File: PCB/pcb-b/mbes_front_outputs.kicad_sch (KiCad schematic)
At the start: 56 parts, among them Q1 BC817, Q11 TPCA8120,L1Q, Q14 BC817, Q15 BC817, Q19 BC817, Q2 BC817, Q20 BC817, Q21 BC817, Q4 TPCA8120,L1Q, Q5 TPCA8120,L1Q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

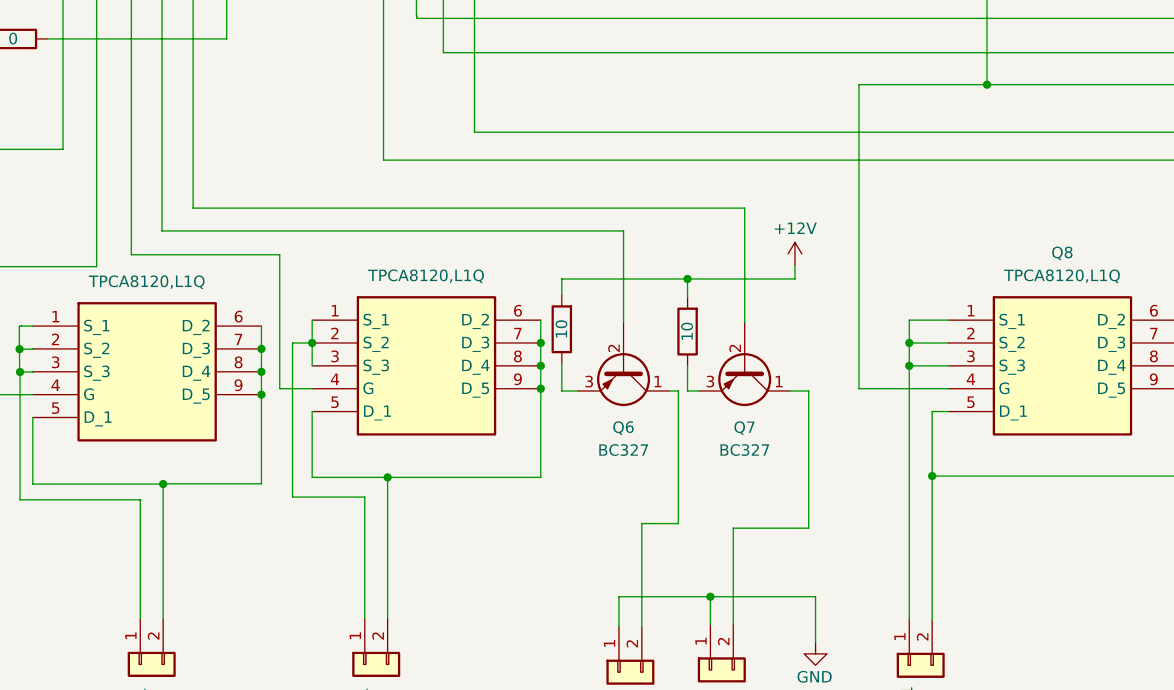
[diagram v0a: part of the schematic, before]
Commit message: Enhancement for direction-indicators circuit
To make the circuit completely safe, I have added MSMF050-2 restatable-fuses to protect it vs short-circuits events.
In order to prevent PNP transistors damages, I have also added a 3 Ohm 0.5W resistor composed by four 1206 SMD componets
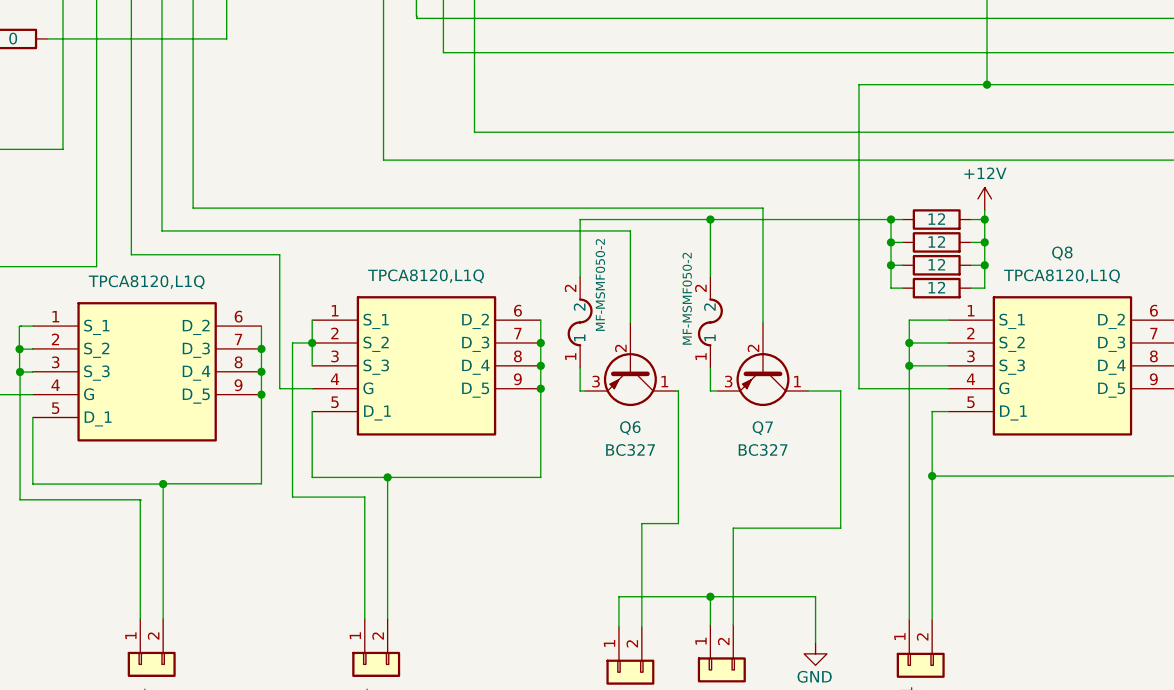
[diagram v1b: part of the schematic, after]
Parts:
- added F1, F2: MF-MSMF050-2, MSMF050-2:FUSE_F050-2, symbol MSMF050-2:MF-MSMF050-2
- added RA30, RA31: 12, Resistor_SMD:R_1206_3216Metric, symbol Device:R
- RA23, RA29: value 10 -> 12; footprint Resistor_THT:R_Axial_DIN0309_L9.0mm_D3.2mm_P12.70mm_Horizontal -> Resistor_SMD:R_1206_3216Metric
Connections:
- net +12V: now also RA30.2, RA31.2
- net at RA23.1: now also RA29.1, F1.2, F2.2, RA30.1, RA31.1; no longer Q7.3 (E)
- net at Q6.3 (E): now also F1.1; no longer RA29.1
- new net: F2.1, Q7.3 (E)
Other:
- moved on the sheet: Q6, Q7

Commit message: Fixes and changes
- 8pin pin-header connectors have been replaced with more standard 10pin connectors
- Wrong components sizes have been fixed
- too small solder-wire connectors have been fixed
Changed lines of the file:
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@@
 (kicad_sch
-	(version 20231120)
+	(version 20250114)
 	(generator "eeschema")
-	(generator_version "8.0")
+	(generator_version "9.0")
 	(paper "A4")
+	(text "LED's resistor depends by the\nled type you are using"
+		(exclude_from_sim no)
+		(at 47.7012 41.5544 90)
+		(effects
+			(font
+				(size 1 1)
+				(italic yes)
+			)
+			(justify left bottom)
+		)
+	)
+	(text "1) addLight\n2) upLight\n3) downLight\n4) leftArrow\n5) rightArrow\n6) neutral\n7) NC\n8) +12V"
+		(exclude_from_sim no)
+		(at 17.145 61.341 0)
+		(effects
+			(font
+				(size 1.27 1.27)
+			)
+			(justify left bottom)
+		)
+	)
 	(junction
 		(at 187.452 76.9112)
@@
 		)
 	)
-	(text "LED's resistor depends by the\nled type you are using"
-		(exclude_from_sim no)
-		(at 47.7012 41.5544 90)
-		(effects
-			(font
-				(size 1 1)
-				(italic yes)
-			)
-			(justify left bottom)
-		)
-	)
-	(text "1) addLight\n2) upLight\n3) downLight\n4) leftArrow\n5) rightArrow\n6) neutral\n7) NC\n8) +12V"
-		(exclude_from_sim no)
-		(at 17.145 61.341 0)
-		(effects
-			(font
-				(size 1.27 1.27)
-			)
-			(justify left bottom)
-		)
-	)

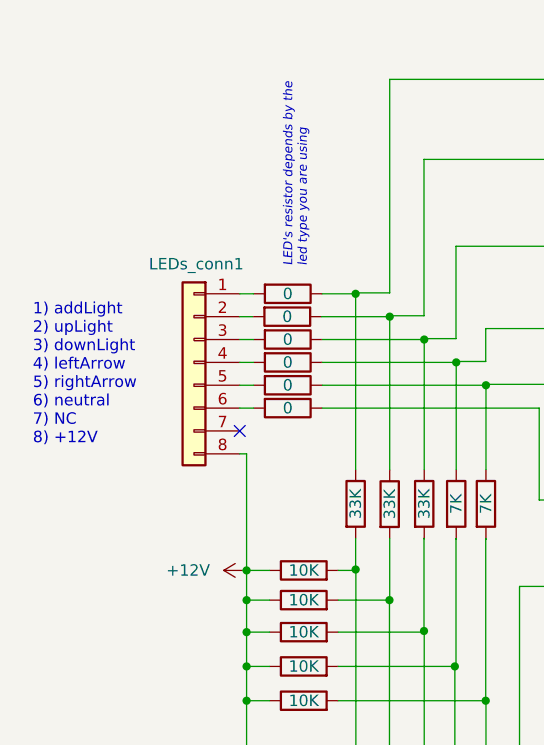
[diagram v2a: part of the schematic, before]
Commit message: Fix: not common connector has been replaced
The 8-pin flat-cable connector is not easy to find on market. It has been replaced with the 10-pin standard one
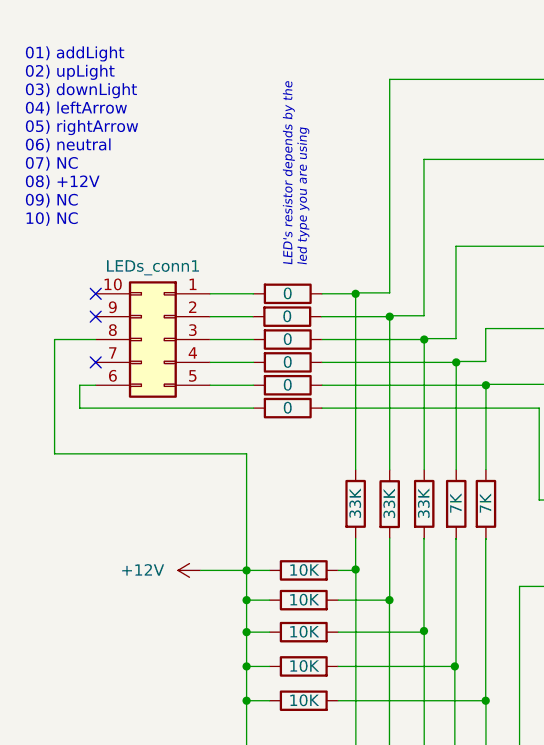
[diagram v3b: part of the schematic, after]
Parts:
- removed LEDs_conn1: Conn_01x08, Connector_PinHeader_2.54mm:PinHeader_2x04_P2.54mm_Vertical, symbol Connector_Generic:Conn_01x08
- added LEDs_conn1: Conn_02x05_Counter_Clockwise, Connector_PinHeader_2.54mm:PinHeader_2x05_P2.54mm_Vertical, symbol Connector_Generic:Conn_02x05_Counter_Clockwise
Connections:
- net +12V: now also LEDs_conn1.8 (Pin_8)
- net at RA1.2: now also LEDs_conn1.1 (Pin_1)
- net at RA2.2: now also LEDs_conn1.2 (Pin_2)
- net at RA3.2: now also LEDs_conn1.3 (Pin_3)
- net at RA4.2: now also LEDs_conn1.4 (Pin_4)
- net at RA5.2: now also LEDs_conn1.5 (Pin_5)
- net at RA6.2: now also LEDs_conn1.6 (Pin_6)
- no-connect marks 1 -> 3
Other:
- note added: "01) addLight 02) upLight 03) downLight 04) leftArrow 05) rightArrow 06) neutral 07) NC 08) +12V 09) NC 10) NC"
- note removed: "1) addLight 2) upLight 3) downLight 4) leftArrow 5) rightArrow 6) neutral 7) NC 8) +12V"

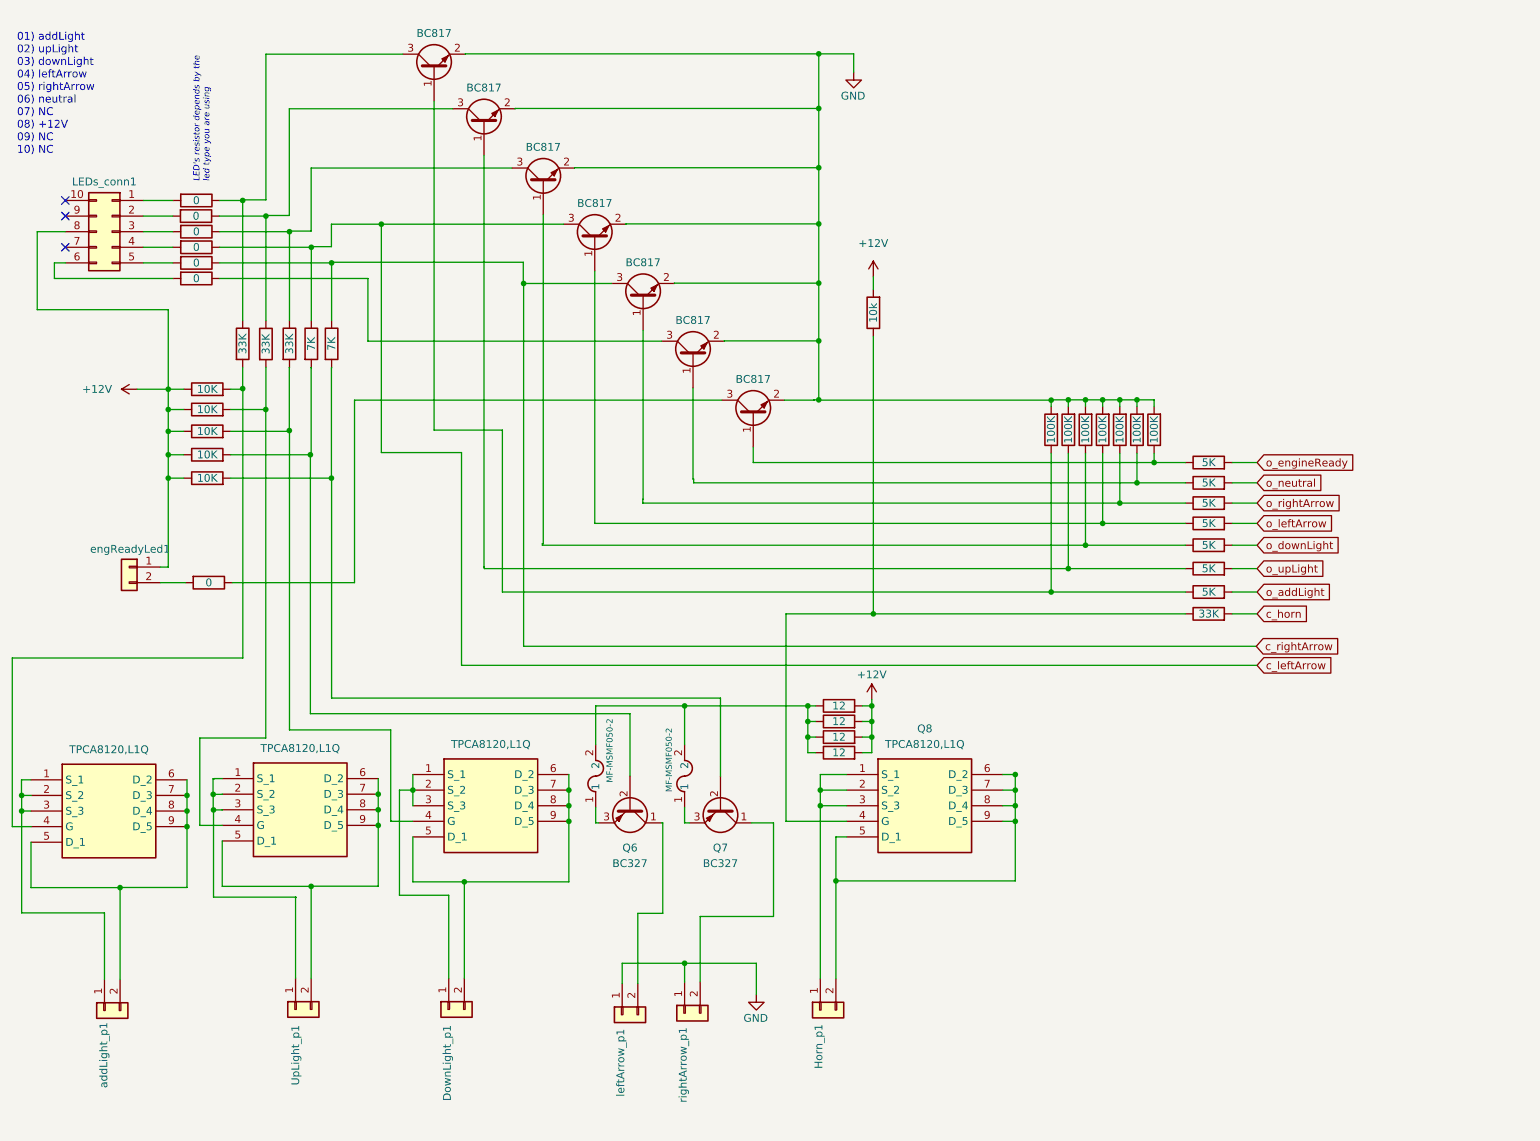
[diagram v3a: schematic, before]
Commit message: Fix stupid error on the direction indicators management
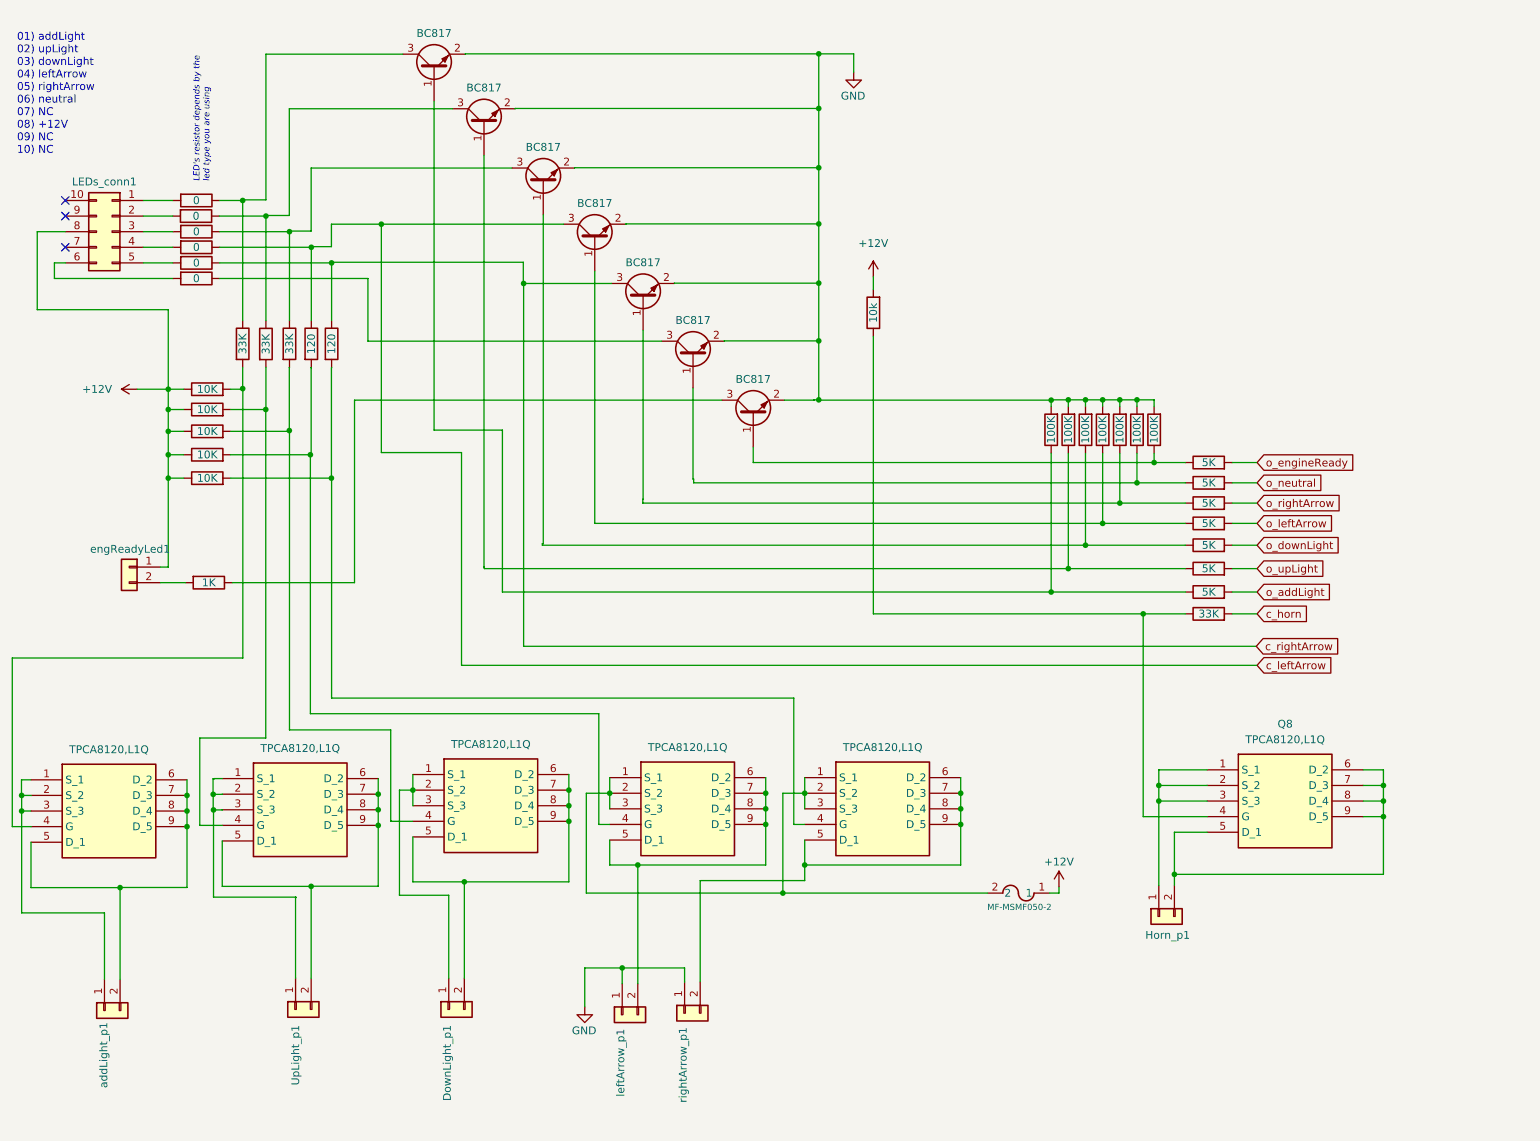
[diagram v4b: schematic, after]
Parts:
- removed F1: MF-MSMF050-2, MSMF050-2:FUSE_F050-2, symbol MSMF050-2:MF-MSMF050-2
- removed Q6, Q7: BC327, Package_TO_SOT_THT:TO-92_Inline_Wide, symbol Transistor_BJT:BC327
- removed RA23, RA29, RA30, RA31: 12, Resistor_SMD:R_1206_3216Metric, symbol Device:R
- added Q6, Q7: TPCA8120,L1Q, TPCA80120:TPH4R003NLL1Q, symbol TPCA8120-LQ:TPCA8120,L1Q
- Q11, Q4, Q5, Q8: footprint TPCA8120:TPH4R003NLL1Q -> TPCA80120:TPH4R003NLL1Q
- RA13, RA14: value 7K -> 120
- RA9: value 0 -> 1K
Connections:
- net +12V: now also F2.1
- net at F2.2: now also Q6.1 (S_1), Q6.2 (S_2), Q6.3 (S_3), Q7.1 (S_1), Q7.2 (S_2), Q7.3 (S_3)
- net at rightArrow_p1.2 (Pin_2): now also Q7.5 (D_1), Q7.6 (D_2), Q7.7 (D_3), Q7.8 (D_4), Q7.9 (D_5)
- net at RA13.2, RA27.2: now also Q6.4 (G)
- net at RA14.2, RA28.2: now also Q7.4 (G)
- net at leftArrow_p1.2 (Pin_2): now also Q6.5 (D_1), Q6.6 (D_2), Q6.7 (D_3), Q6.8 (D_4), Q6.9 (D_5)
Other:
- moved on the sheet: Horn_p1, Q8

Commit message: Fix: horn still usable also when the mb is off
Horn is enabled by tempPower, now
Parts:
- added Q10: BC817, Package_TO_SOT_SMD:SOT-23, symbol Transistor_BJT:BC817
- added RA23: 20K, Resistor_SMD:R_1206_3216Metric, symbol Device:R
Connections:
- net c_horn: now also Q10.2 (E); no longer RA7.2
- net at Q8.4 (G), RA7.1: no longer RA42.1
- new net: Q10.3 (C), RA42.1, RA7.2
- new net: Q10.1 (B), RA23.2
- new net tempPower: RA23.1

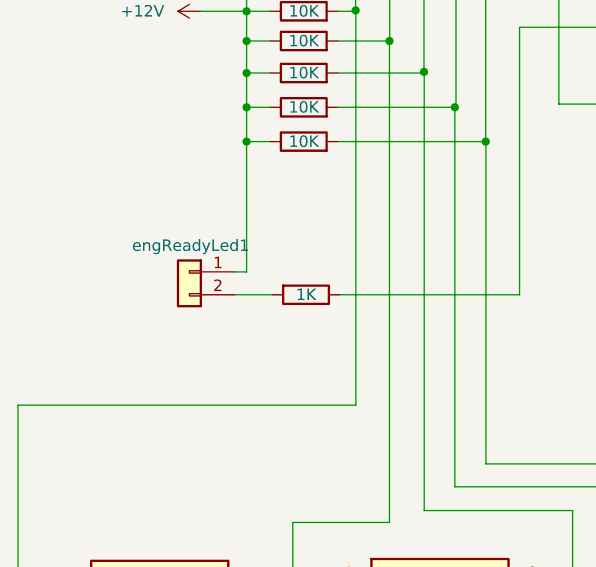
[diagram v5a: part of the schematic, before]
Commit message: Wrong EngReady_LED connector orientation fixed
Standard: 1=negative 2=positive
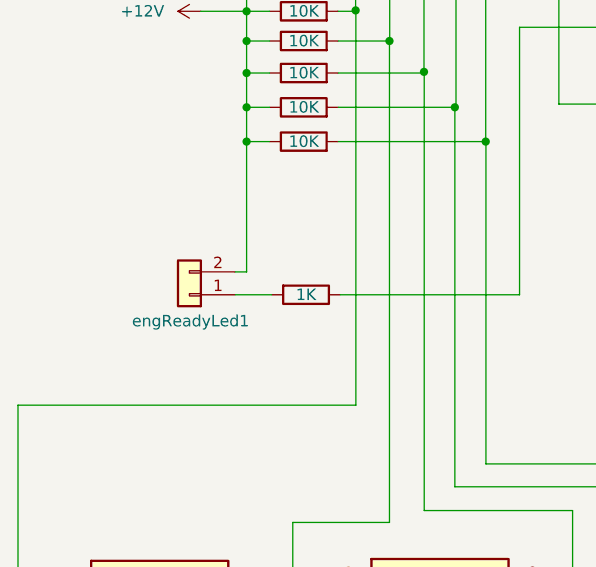
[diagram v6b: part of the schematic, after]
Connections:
- net +12V: now also engReadyLed1.2 (Pin_2); no longer engReadyLed1.1 (Pin_1)
- net at RA9.2: now also engReadyLed1.1 (Pin_1); no longer engReadyLed1.2 (Pin_2)
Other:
- moved on the sheet: engReadyLed1
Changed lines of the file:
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@@
 	(symbol
 		(lib_id "Connector_Generic:Conn_01x02")
-		(at 34.544 104.14 0)
-		(mirror y)
+		(at 34.544 106.68 180)
 		(unit 1)
 		(exclude_from_sim no)
@@
 		(dnp no)
 		(property "Reference" "engReadyLed1"
-			(at 34.671 101.219 0)
+			(at 34.671 109.601 0)
 			(effects
 				(font
@@
 		)
 		(property "Value" "Conn_01x02"
-			(at 34.544 100.584 0)
+			(at 34.544 110.236 0)
 			(effects
 				(font
@@
 		)
 		(property "Footprint" "Connector_PinHeader_2.54mm:PinHeader_1x02_P2.54mm_Vertical"
-			(at 34.544 104.14 0)
+			(at 34.544 106.68 0)
 			(effects
 				(font
@@
 		)
 		(property "Datasheet" "~"
-			(at 34.544 104.14 0)
+			(at 34.544 106.68 0)
 			(effects
 				(font
@@
 		)
 		(property "Description" ""
-			(at 34.544 104.14 0)
+			(at 34.544 106.68 0)
 			(effects
 				(font
